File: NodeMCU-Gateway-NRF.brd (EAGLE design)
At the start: 59.7 x 40.6 mm, 28 parts, among them IC1 ATSHA204A, J2 GROVE-I2C, J3 Lipo Battery, J5 CON_HEADER_1X08-PTH, P1 PADSMALL, P2 PADNORMAL

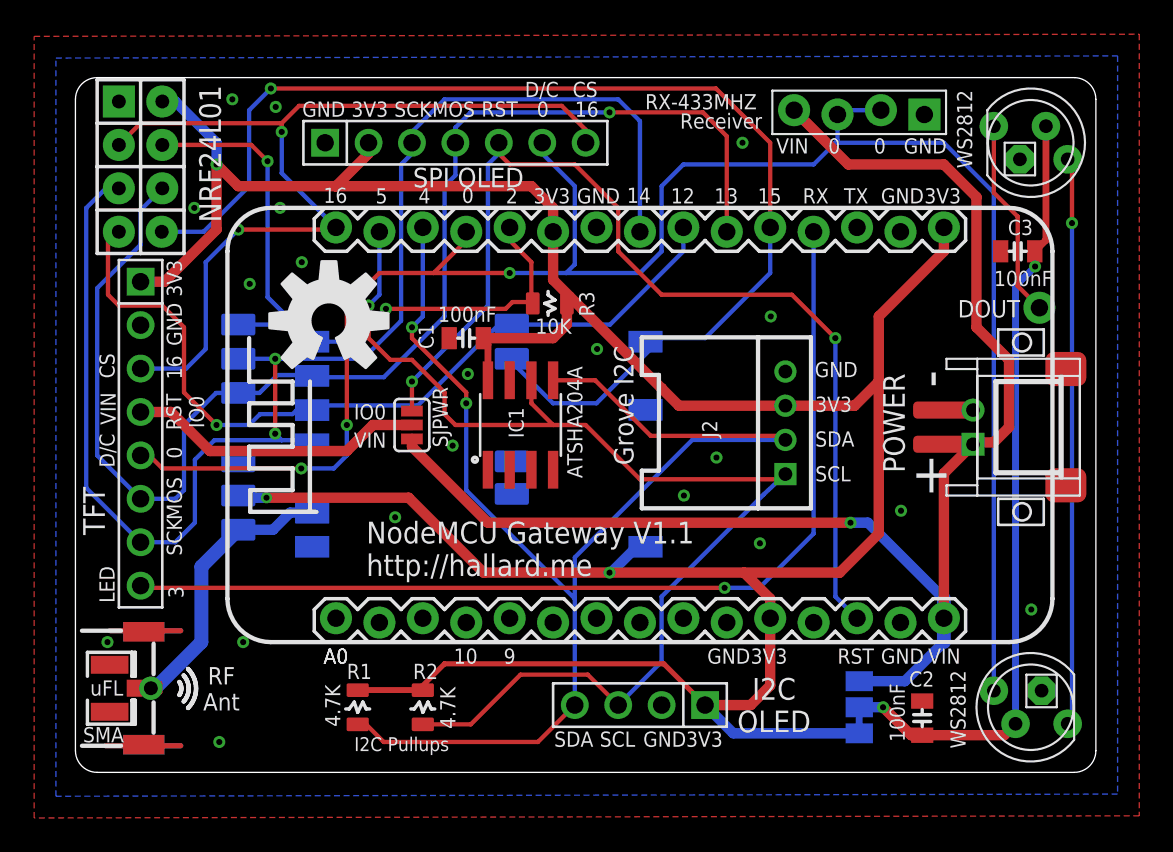
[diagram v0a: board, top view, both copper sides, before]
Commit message: Silk error
Silk SJPWR is not tied to GPIO0 but RST/VIN
Increased SJPWR size for easy soldering
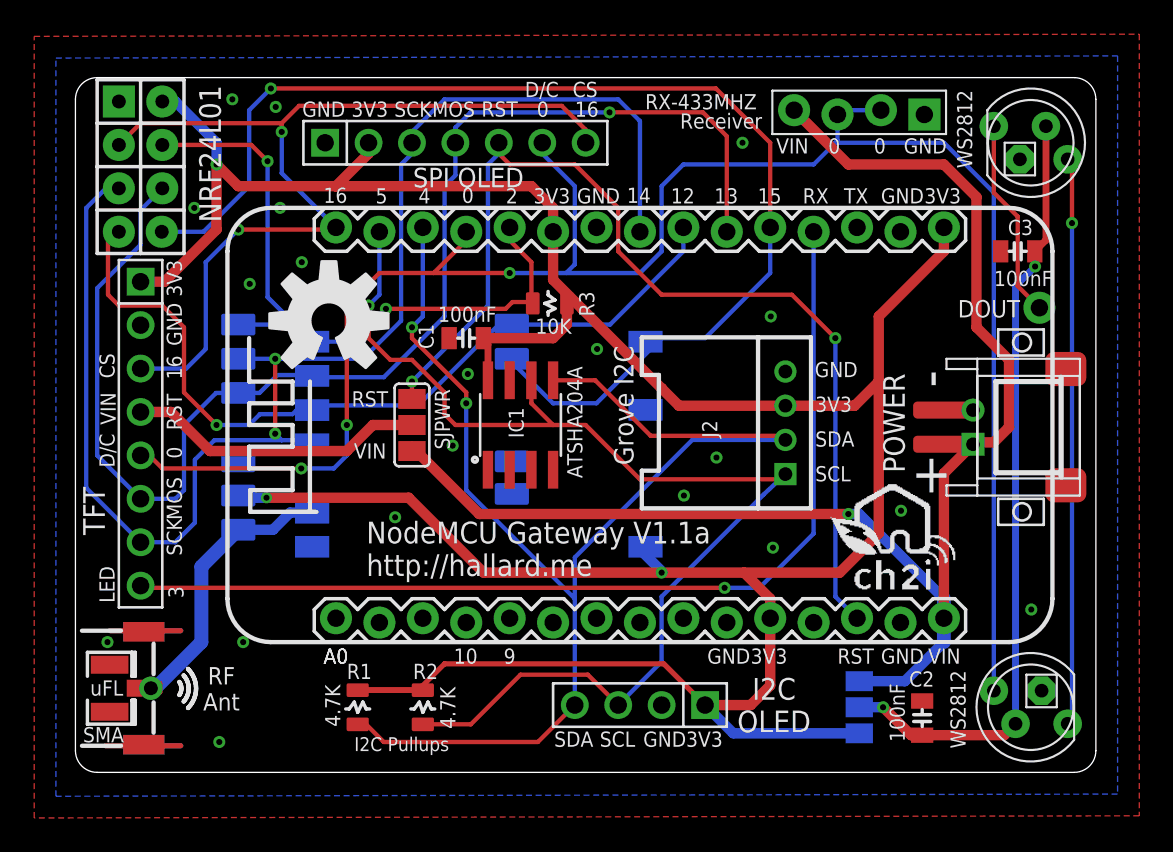
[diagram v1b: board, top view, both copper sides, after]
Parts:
- added U$6, U$7: (no value), _c2h:LOGO_CH2I_75MM
- SJPWR: device SparkFun-Passives:PAD-JUMPER-3-NO_YES_SILK -> SparkFun-Passives:PAD-JUMPER-3-2OF3_NC_BY_TRACE_YES_SILK_LARGE
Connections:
- net SS renamed GPIO15
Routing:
- net RST: track 61.0 -> 60.3 mm
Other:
- board text added: "NodeMCU Gateway V1.1a http://hallard.me"
- board text removed: "IO0"
- board text removed: "NodeMCU Gateway V1.1 http://hallard.me"
- board text removed: "RST IO0"
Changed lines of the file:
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@@
 <setting verticaltext="up"/>
 </settings>
-<grid distance="25" unitdist="mil" unit="mil" style="lines" multiple="1" display="yes" altdistance="5" altunitdist="mil" altunit="mil"/>
+<grid distance="50" unitdist="mil" unit="mil" style="lines" multiple="1" display="yes" altdistance="5" altunitdist="mil" altunit="mil"/>
 <layers>
 <layer number="1" name="Top" color="4" fill="1" visible="yes" active="yes"/>
@@
 <text x="5.4345" y="10.892" size="0.889" layer="25" font="vector" ratio="15" rot="R270">3</text>
 <text x="1.40225" y="19.81375" size="0.889" layer="25" font="vector" ratio="15" rot="R270">D/C</text>
-<text x="6.41875" y="21.08375" size="0.889" layer="25" font="vector" ratio="15" rot="R270" align="center">RST
-IO0</text>
+<text x="5.78375" y="21.08375" size="0.889" layer="25" font="vector" ratio="15" rot="R270" align="center">RST</text>
 <text x="1.40225" y="24.51275" size="0.889" layer="25" font="vector" ratio="15" rot="R270">CS</text>
 <text x="29.08125" y="39.50225" size="0.889" layer="25" font="vector" ratio="15">CS</text>
@@
 <wire x1="58.42" y1="40.64" x2="59.69" y2="39.37" width="0" layer="20" curve="-90"/>
 <text x="38.66975" y="35.88275" size="1.27" layer="26" font="vector" ratio="15" rot="MR180">RX-Receiver</text>
-<text x="35.36775" y="14.03875" size="1.27" layer="26" font="vector" ratio="15" rot="MR180">NodeMCU Gateway V1.1
+<text x="34.85975" y="14.03875" size="1.27" layer="26" font="vector" ratio="15" rot="MR180">NodeMCU Gateway V1.1a
 http://hallard.me</text>
 <text x="29.33525" y="33.27925" size="0.889" layer="25" font="vector" ratio="15">GND</text>
@@
 <text x="22.128" y="6.35525" size="0.889" layer="25" font="vector" ratio="15">10</text>
 <text x="25.049" y="6.35525" size="0.889" layer="25" font="vector" ratio="15">9</text>
-<text x="17.01975" y="11.48825" size="1.27" layer="25" font="vector" ratio="15">NodeMCU Gateway V1.1
+<text x="17.01975" y="11.48825" size="1.27" layer="25" font="vector" ratio="15">NodeMCU Gateway V1.1a
 http://hallard.me</text>
 <text x="51.7825" y="6.48225" size="0.889" layer="26" font="vector" ratio="15" rot="MR0">VIN</text>
@@
 <text x="49.306" y="4.95825" size="0.889" layer="26" font="vector" ratio="15" rot="MR0">VIN</text>
 <text x="1.46575" y="22.22675" size="0.889" layer="25" font="vector" ratio="15" rot="R270">VIN</text>
-<text x="16.286" y="20.64275" size="0.889" layer="25" font="vector" ratio="15">IO0</text>
-<text x="16.286" y="18.99175" size="0.889" layer="25" font="vector" ratio="15">VIN</text>
-<text x="5.8155" y="21.21075" size="0.889" layer="26" font="vector" ratio="15" rot="MR90" align="center">RST
-IO0</text>
+<text x="16.159" y="21.40475" size="0.889" layer="25" font="vector" ratio="15">RST</text>
+<text x="16.286" y="18.35675" size="0.889" layer="25" font="vector" ratio="15">VIN</text>
+<text x="5.8155" y="21.21075" size="0.889" layer="26" font="vector" ratio="15" rot="MR90" align="center">RST</text>
 <wire x1="2.667" y1="8.28675" x2="0.381" y2="8.28675" width="0.254" layer="22"/>
 <wire x1="0.381" y1="1.55575" x2="2.667" y2="1.55575" width="0.254" layer="22"/>
@@
 <attribute name="VALUE" x="29.0195" y="26.543" size="0.889" layer="25" font="vector" ratio="15" rot="R180"/>
 </element>
-<element name="SJPWR" library="SparkFun-Passives" package="PAD-JUMPER-3-NO_YES_SILK" value="" x="19.685" y="20.32" smashed="yes" rot="R90">
-<attribute name="NAME" x="20.8915" y="22.5425" size="0.889" layer="25" font="vector" ratio="15" rot="R270"/>
+<element name="SJPWR" library="SparkFun-Passives" package="PAD-JUMPER-3-2OF3_NC_BY_TRACE_YES_SILK_LARGE" value="" x="19.685" y="20.32" smashed="yes" rot="R90">
+<attribute name="NAME" x="21.0185" y="22.4155" size="0.889" layer="25" font="vector" ratio="15" rot="R270"/>
 <attribute name="VALUE" x="19.685" y="20.2199" size="0.02" layer="27" rot="R90"/>
 <attribute name="VALUE" x="21.59" y="19.05" size="0.4064" layer="27" rot="R90"/>
@@
 <attribute name="VALUE" x="7.239" y="40.1955" size="1.27" layer="25" font="vector" ratio="15" rot="R270"/>
 </element>
+<element name="U$6" library="_c2h" package="LOGO_CH2I_75MM" value="" x="48.26" y="12.7"/>
+<element name="U$7" library="_c2h" package="LOGO_CH2I_75MM" value="" x="21.336" y="2.794" rot="MR0"/>
 </elements>
 <signals>
@@
 <via x="30.51175" y="24.765" extent="1-16" drill="0.3556" diameter="0.7112"/>
 <via x="37.49675" y="18.415" extent="1-16" drill="0.3556" diameter="0.7112"/>
-<via x="40.03675" y="13.3985" extent="1-16" drill="0.3556" diameter="0.7112"/>
+<via x="40.79875" y="13.1445" extent="1-16" drill="0.3556" diameter="0.7112"/>
 <contactref element="RADIO1" pad="1"/>
 <via x="22.95525" y="23.3045" extent="1-16" drill="0.3556" diameter="0.7112"/>
@@
 <wire x1="1.27" y1="18.542" x2="3.81" y2="16.002" width="0.254" layer="16"/>
 </signal>
-<signal name="SS">
+<signal name="GPIO15">
 <contactref element="JP2" pad="11"/>
 <contactref element="U$3" pad="DIO0"/>
@@
 <contactref element="R2" pad="2"/>
 <contactref element="R1" pad="2"/>
-<via x="31.242" y="11.684" extent="1-16" drill="0.3556" diameter="0.7112" alwaysstop="yes"/>
+<via x="34.29" y="11.684" extent="1-16" drill="0.3556" diameter="0.7112"/>
 <contactref element="J5" pad="1"/>
 <contactref element="JP2" pad="6"/>
@@
 <wire x1="21.59" y1="6.35" x2="34.417" y2="6.35" width="0.3048" layer="1"/>
 <wire x1="34.417" y1="6.35" x2="36.83" y2="3.937" width="0.3048" layer="1"/>
-<wire x1="31.242" y1="11.684" x2="39.116" y2="11.684" width="0.6096" layer="1"/>
-<wire x1="31.242" y1="11.684" x2="23.876" y2="11.684" width="0.6096" layer="1"/>
+<wire x1="34.29" y1="11.684" x2="39.116" y2="11.684" width="0.6096" layer="1"/>
+<wire x1="34.29" y1="11.684" x2="23.876" y2="11.684" width="0.6096" layer="1"/>
 <wire x1="32.851" y1="13.208" x2="33.344" y2="13.193" width="0.6096" layer="16"/>
 <contactref element="J2" pad="3"/>
@@
 <wire x1="41.529" y1="21.447" x2="45.577" y2="21.447" width="0.6096" layer="1"/>
 <wire x1="45.577" y1="21.447" x2="46.99" y2="22.86" width="0.6096" layer="1"/>
-<wire x1="31.242" y1="11.684" x2="31.327" y2="11.684" width="0.6096" layer="16"/>
-<wire x1="31.327" y1="11.684" x2="32.851" y2="13.208" width="0.6096" layer="16"/>
+<wire x1="34.29" y1="11.684" x2="34.375" y2="11.684" width="0.6096" layer="16"/>
+<wire x1="34.375" y1="11.684" x2="32.851" y2="13.208" width="0.6096" layer="16"/>
 <wire x1="28.7495" y1="27.432" x2="29.321" y2="27.432" width="0.254" layer="1"/>
 <wire x1="29.321" y1="27.432" x2="29.6465" y2="27.1065" width="0.254" layer="1"/>
@@
 <wire x1="44.45" y1="10.287" x2="45.72" y2="9.017" width="0.254" layer="16"/>
 <wire x1="24.13" y1="27.305" x2="19.685" y2="22.86" width="0.254" layer="16"/>
-<wire x1="19.685" y1="21.1328" x2="19.685" y2="22.86" width="0.254" layer="1"/>
+<wire x1="19.685" y1="21.844" x2="19.685" y2="22.86" width="0.254" layer="1"/>
 </signal>
 <signal name="VLED">
@@
 <contactref element="SJLED" pad="1"/>
 <wire x1="45.847" y1="5.334" x2="48.514" y2="5.334" width="0.6096" layer="16"/>
-<via x="45.339" y="14.605" extent="1-16" drill="0.3556" diameter="0.7112"/>
-<wire x1="24.13" y1="14.605" x2="45.339" y2="14.605" width="0.6096" layer="1"/>
-<wire x1="45.339" y1="14.605" x2="46.355" y2="14.605" width="0.6096" layer="16"/>
-<wire x1="46.355" y1="14.605" x2="50.8" y2="10.16" width="0.6096" layer="16"/>
+<via x="45.212" y="15.113" extent="1-16" drill="0.3556" diameter="0.7112"/>
+<wire x1="23.622" y1="15.113" x2="45.212" y2="15.113" width="0.6096" layer="1"/>
+<wire x1="45.212" y1="15.113" x2="45.847" y2="15.113" width="0.6096" layer="16"/>
+<wire x1="45.847" y1="15.113" x2="50.8" y2="10.16" width="0.6096" layer="16"/>
 <wire x1="50.8" y1="10.16" x2="50.8" y2="9.017" width="0.8128" layer="16"/>
-<wire x1="24.13" y1="14.605" x2="19.685" y2="19.05" width="0.6096" layer="1"/>
-<wire x1="19.685" y1="19.05" x2="19.685" y2="19.5072" width="0.6096" layer="1"/>
+<wire x1="23.622" y1="15.113" x2="19.685" y2="19.05" width="0.6096" layer="1"/>
+<wire x1="19.685" y1="19.05" x2="19.685" y2="18.796" width="0.6096" layer="1"/>
 </signal>
 </signals>

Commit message: Version 1.1b
NRF24L01 wiring same as mysensor gateway
Added place to add cap near NRF24L01
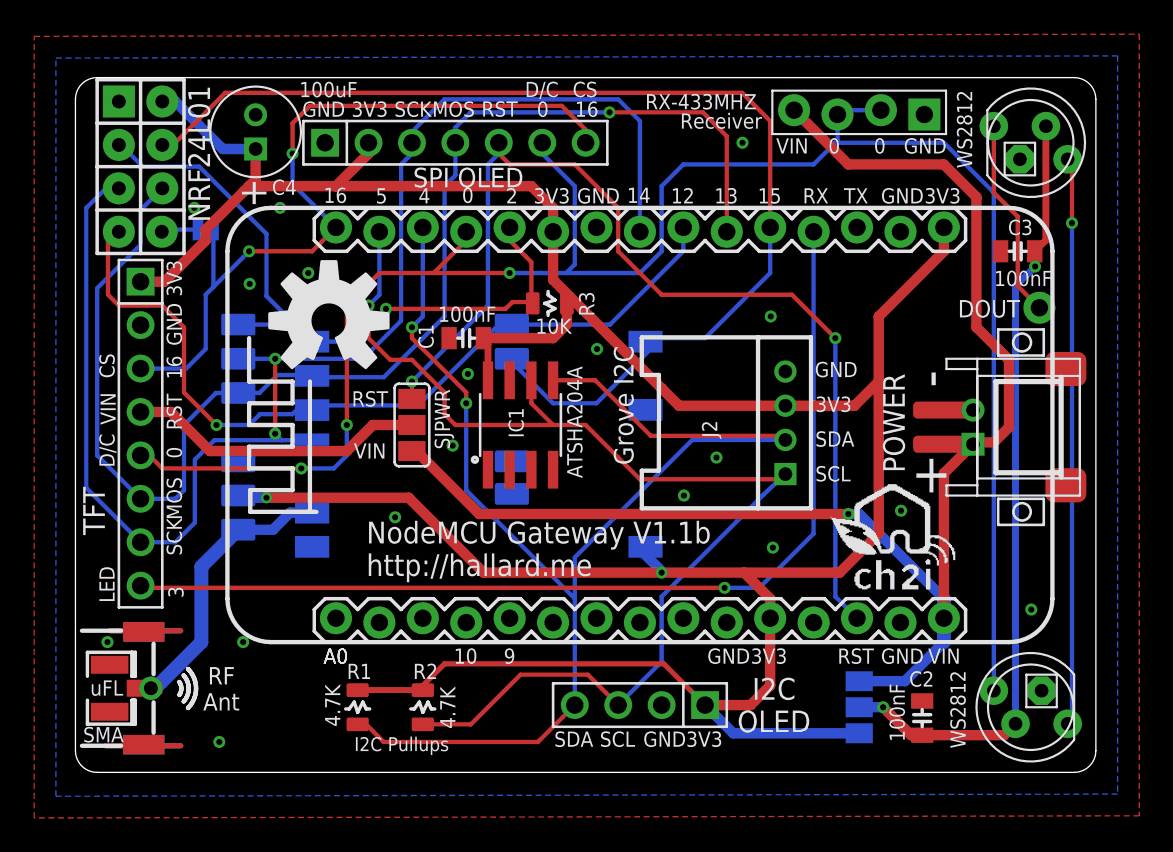
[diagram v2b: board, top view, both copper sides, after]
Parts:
- added C4: 100uF, Seeed-OPL-Discrete:RADIAL-2.0-D5.0*H7MM
- added SNRFIRQ: NRFIRQ, SparkFun-Passives:PAD-JUMPER-2-NO_YES_SILK
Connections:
- new net N$4: RADIO1.8, SNRFIRQ.1
- net 3V3: now also C4.+
- net GND: now also C4.-
- net GPIO15: now also RADIO1.4; no longer RADIO1.8
- net GPIO16: now also SNRFIRQ.2; no longer RADIO1.3
- net GPIO2: now also RADIO1.3; no longer RADIO1.4
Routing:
- net GPIO16: track 54.8 -> 46.1 mm
- net GPIO15: track 71.1 -> 66.9 mm, vias 1 -> 0
- net N$4: track 0.00 -> 2.17 mm
- net 3V3: track 185.4 -> 186.0 mm, vias 3 -> 2
- net GPIO2: vias 2 -> 1
- net GND: vias 20 -> 18
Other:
- board text added: "NodeMCU Gateway V1.1b http://hallard.me"
- board text removed: "NodeMCU Gateway V1.1a http://hallard.me"
